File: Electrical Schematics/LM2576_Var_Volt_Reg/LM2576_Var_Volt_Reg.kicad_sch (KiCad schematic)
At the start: 10 parts, among them J1 Conn_01x03_Pin, U1 LM2576S-12

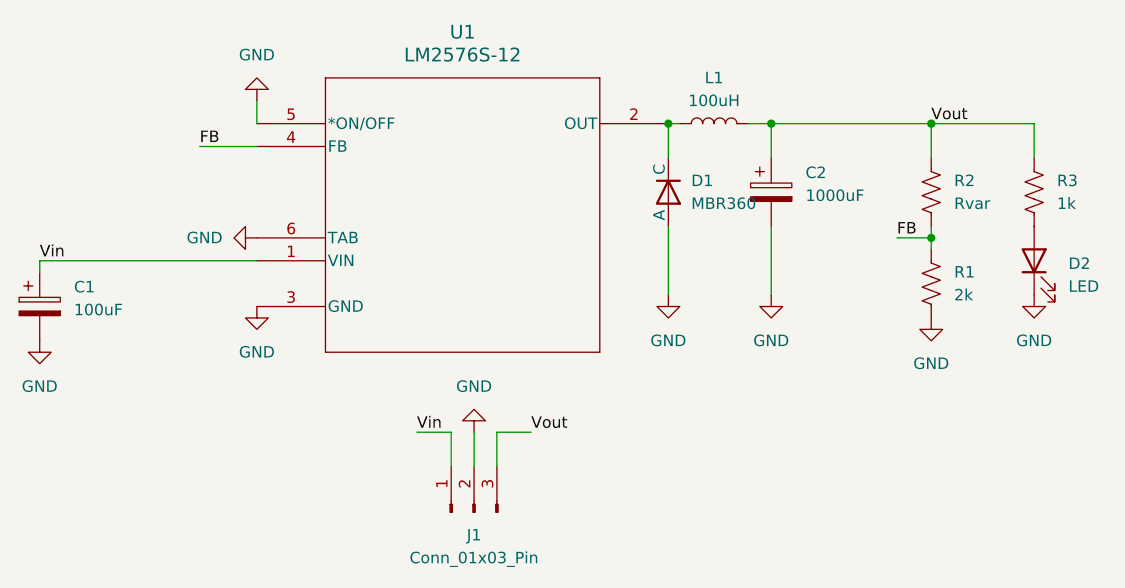
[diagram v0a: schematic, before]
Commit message: added lm2679
Updated LM2576 schematic and started creating PCB layout
Created LM2679 Schematic
Updated some slicer code to open config file more easily when only main is open
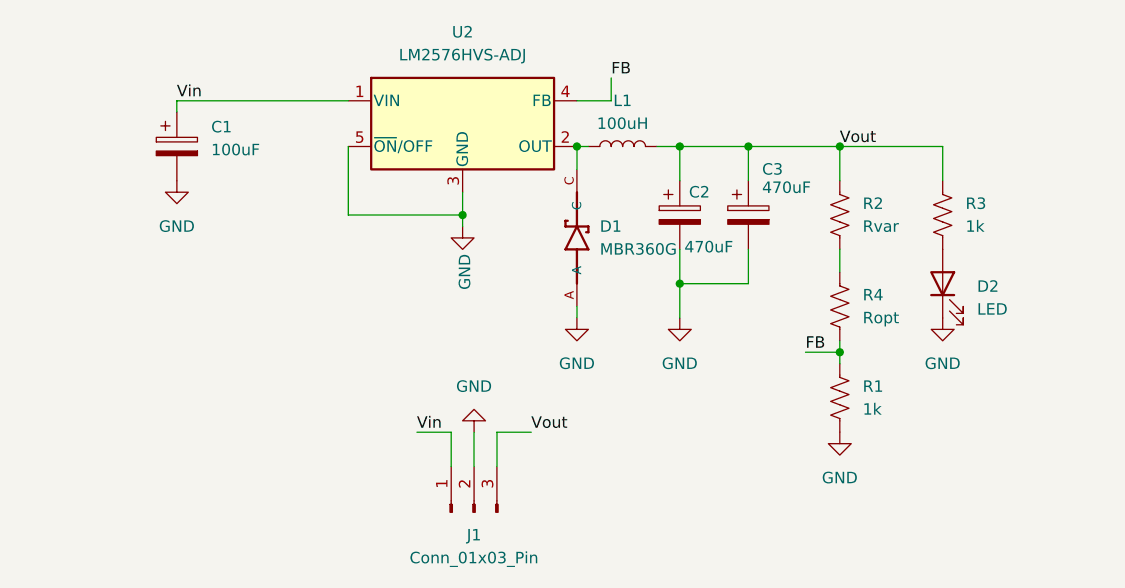
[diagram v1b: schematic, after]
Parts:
- removed D1: MBR360, symbol MBR360:Diode
- removed U1: LM2576S-12, TS5B_TEX, symbol LM2576ADJ:LM2576S-12
- added C3: 470uF, Capacitor_THT:CP_Radial_D7.5mm_P2.50mm, symbol Device:C_Polarized
- added D1: MBR360G, MBR360:DIOAD950W125L840D505, symbol MBR360G:MBR360G
- added R4: Ropt, Resistor_SMD:R_1206_3216Metric_Pad1.30x1.75mm_HandSolder, symbol Device:R_US
- added U2: LM2576HVS-ADJ, Package_TO_SOT_SMD:TO-263-5_TabPin3, symbol Regulator_Switching:LM2576HVS-ADJ
- C1: footprint (none) -> Capacitor_THT:CP_Radial_D6.3mm_P2.50mm
- C2: value 1000uF -> 470uF; footprint (none) -> Capacitor_THT:CP_Radial_D7.5mm_P2.50mm
- D2: footprint (none) -> LED_SMD:LED_0805_2012Metric_Pad1.15x1.40mm_HandSolder
- J1: footprint Connector_PinHeader_1.00mm:PinHeader_1x03_P1.00mm_Vertical -> Connector_PinSocket_2.54mm:PinSocket_1x03_P2.54mm_Vertical
- L1: footprint Inductor_SMD:L_1206_3216Metric_Pad1.22x1.90mm_HandSolder -> Inductor_THT:L_Toroid_Vertical_L21.6mm_W9.5mm_P7.11mm_Pulse_C
- R1: value 2k -> 1k; footprint (none) -> Resistor_SMD:R_1206_3216Metric
- R2: footprint (none) -> Resistor_SMD:R_1206_3216Metric_Pad1.30x1.75mm_HandSolder
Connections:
- net FB: now also R4.2, U2.4 (FB); no longer R2.2
- net GND: now also C3.2, D1.A, U2.3 (GND), U2.5 (~{ON}/OFF)
- net Vin: now also U2.1 (VIN)
- net Vout: now also C3.1
- net at L1.1: now also D1.C, U2.2 (OUT)
- new net: R2.2, R4.1
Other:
- moved on the sheet: C1, C2, D2, L1, R1, R2, R3
